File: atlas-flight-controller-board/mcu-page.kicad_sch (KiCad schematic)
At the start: 1 part

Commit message: finishing up schematic for v1.
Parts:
- renumbered U to U?
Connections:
- net SD_CS: now reaches U?.10 (CS1)
- net MOSI: now reaches U?.11 (MOSI)
- net MISO: now reaches U?.12 (MISO)
- net SCK: now reaches U?.13 (SCK)
- net UART_RFD900_TX_MCU_RX: now reaches U?.34 (RX8)
- net UART_MCU_TX_RFD900_RX: now reaches U?.35 (TX8)
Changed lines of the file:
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@@
 	(generator_version "9.0")
 	(paper "A4")
+	(global_label "UART_RFD900_TX_MCU_RX"
+		(shape input)
+		(at 124.46 83.82 180)
+		(fields_autoplaced yes)
+		(effects
+			(font
+				(size 1.27 1.27)
+			)
+			(justify right)
+		)
+		(property "Intersheetrefs" "${INTERSHEET_REFS}"
+			(at 96.9821 83.82 0)
+			(effects
+				(font
+					(size 1.27 1.27)
+				)
+				(justify right)
+				(hide yes)
+			)
+		)
+	)
+	(global_label "MOSI"
+		(shape input)
+		(at 165.1 101.6 0)
+		(fields_autoplaced yes)
+		(effects
+			(font
+				(size 1.27 1.27)
+			)
+			(justify left)
+		)
+		(property "Intersheetrefs" "${INTERSHEET_REFS}"
+			(at 172.6814 101.6 0)
+			(effects
+				(font
+					(size 1.27 1.27)
+				)
+				(justify left)
+				(hide yes)
+			)
+		)
+	)
 	(global_label "I2C_SDA"
 		(shape input)
@@
 		)
 	)
+	(global_label "UART_MCU_TX_RFD900_RX"
+		(shape input)
+		(at 124.46 86.36 180)
+		(fields_autoplaced yes)
+		(effects
+			(font
+				(size 1.27 1.27)
+			)
+			(justify right)
+		)
+		(property "Intersheetrefs" "${INTERSHEET_REFS}"
+			(at 96.9821 86.36 0)
+			(effects
+				(font
+					(size 1.27 1.27)
+				)
+				(justify right)
+				(hide yes)
+			)
+		)
+	)
 	(global_label "I2C_SCL"
 		(shape input)
@@
 				)
 				(justify right)
+				(hide yes)
+			)
+		)
+	)
+	(global_label "SCK"
+		(shape input)
+		(at 124.46 104.14 180)
+		(fields_autoplaced yes)
+		(effects
+			(font
+				(size 1.27 1.27)
+			)
+			(justify right)
+		)
+		(property "Intersheetrefs" "${INTERSHEET_REFS}"
+			(at 117.7253 104.14 0)
+			(effects
+				(font
+					(size 1.27 1.27)
+				)
+				(justify right)
+				(hide yes)
+			)
+		)
+	)
+	(global_label "MISO"
+		(shape input)
+		(at 165.1 99.06 0)
+		(fields_autoplaced yes)
+		(effects
+			(font
+				(size 1.27 1.27)
+			)
+			(justify left)
+		)
+		(property "Intersheetrefs" "${INTERSHEET_REFS}"
+			(at 172.6814 99.06 0)
+			(effects
+				(font
+					(size 1.27 1.27)
+				)
+				(justify left)
+				(hide yes)
+			)
+		)
+	)
+	(global_label "SD_CS"
+		(shape input)
+		(at 165.1 93.98 0)
+		(fields_autoplaced yes)
+		(effects
+			(font
+				(size 1.27 1.27)
+			)
+			(justify left)
+		)
+		(property "Intersheetrefs" "${INTERSHEET_REFS}"
+			(at 174.0118 93.98 0)
+			(effects
+				(font
+					(size 1.27 1.27)
+				)
+				(justify left)
 				(hide yes)
 			)
@@
 		(dnp no)
 		(fields_autoplaced yes)
-		(property "Reference" "U"
+		(property "Reference" "U?"
 			(at 144.78 33.02 0)
 			(effects
@@
 		(instances
 			(project "atlas-flight-controller-board"
-				(path "/99efb2d6-b5f7-438c-9ed2-f359400f01a1/0e8824f2-4013-4596-998b-cdfa7c1cf328"
-					(reference "U3")
+				(path "/99efb2d6-b5f7-438c-9ed2-f359400f01a1/ebeff960-adac-492b-ba2d-f8a8dedd6bc1"
+					(reference "U?")
 					(unit 1)
 				)

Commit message: wip commit
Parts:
- added J1: UART8 RPI Screw Term, TerminalBlock:TerminalBlock_Xinya_XY308-2.54-2P_1x02_P2.54mm_Horizontal, symbol Connector:Screw_Terminal_01x02
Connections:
- net UART_MCU_TX_RFD900_RX: now also U?.29 (TX7); no longer U?.35 (TX8)
- net UART_RFD900_TX_MCU_RX: now also U?.28 (RX7); no longer U?.34 (RX8)
- net UART_GPS_TX_MCU_RX: now reaches U?.0 (RX1)
- net UART_MCU_TX_GPS_RX: now reaches U?.1 (TX1)
- net GPS_FIX: now reaches U?.2 (OUT2)
- net MAG_INT: now reaches U?.20 (A6)
- net BARO_INT: now reaches U?.21 (A7)
- net IMU_INT1: now reaches U?.22 (A8)
- net IMU_INT2: now reaches U?.23 (A9)
- new net UART_MCU_TX_RPI_RX: J1.1 (Pin_1), U?.35 (TX8)
- new net UART_RPI_TX_MCU_RX: J1.2 (Pin_2), U?.34 (RX8)

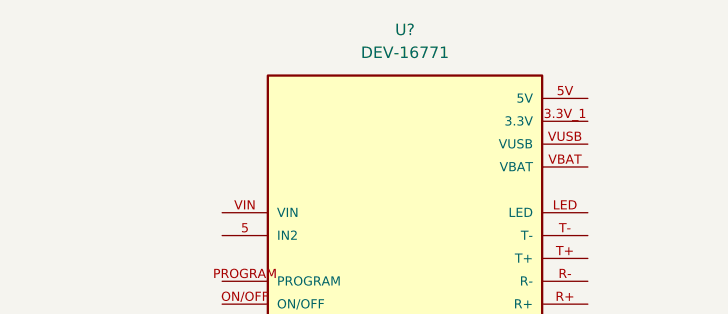
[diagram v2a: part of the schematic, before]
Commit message: Added Regulator, Leaving disconnected, and off pcb for now as teensy board does this automatically. Leaving on for future revs without teensy board
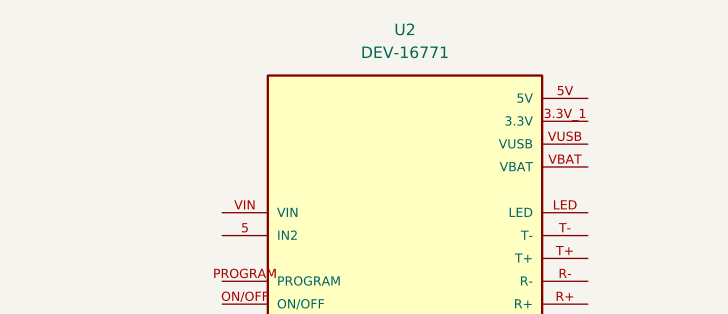
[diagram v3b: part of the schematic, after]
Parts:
- U2: renamed from U?; footprint DEV-16771:MODULE_DEV-16771 -> Teensy4.1:MODULE_DEV-16771
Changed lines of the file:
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@@
 		(dnp no)
 		(fields_autoplaced yes)
-		(property "Reference" "U?"
+		(property "Reference" "U2"
 			(at 144.78 33.02 0)
 			(effects
@@
 			)
 		)
-		(property "Footprint" "DEV-16771:MODULE_DEV-16771"
+		(property "Footprint" "Teensy4.1:MODULE_DEV-16771"
 			(at 144.78 88.9 0)
 			(effects
@@
 			(project "atlas-flight-controller-board"
 				(path "/99efb2d6-b5f7-438c-9ed2-f359400f01a1/ebeff960-adac-492b-ba2d-f8a8dedd6bc1"
-					(reference "U?")
+					(reference "U2")
 					(unit 1)
 				)

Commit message: Updating IMU to SPI
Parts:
- removed J1: UART8 RPI Screw Term, TerminalBlock:TerminalBlock_Xinya_XY308-2.54-2P_1x02_P2.54mm_Horizontal, symbol Connector:Screw_Terminal_01x02
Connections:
- net UART_MCU_TX_RPI_RX: no longer names the net of U2.35 (TX8)
- net UART_RPI_TX_MCU_RX: no longer names the net of U2.34 (RX8)
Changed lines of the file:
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@@
 	(generator_version "9.0")
 	(paper "A4")
-	(junction
-		(at 124.46 83.82)
-		(diameter 0)
-		(color 0 0 0 0)
-	)
-	(junction
-		(at 124.46 86.36)
-		(diameter 0)
-		(color 0 0 0 0)
-	)
 	(wire
 		(pts
-			(xy 74.93 86.36) (xy 124.46 86.36)
+			(xy 129.54 83.82) (xy 124.46 83.82)
 		)
 		(stroke
@@
 	(wire
 		(pts
-			(xy 129.54 83.82) (xy 124.46 83.82)
+			(xy 129.54 86.36) (xy 124.46 86.36)
 		)
 		(stroke
 			(width 0)
 			(type default)
-		)
-	)
-	(wire
-		(pts
-			(xy 129.54 86.36) (xy 124.46 86.36)
-		)
-		(stroke
-			(width 0)
-			(type default)
-		)
-	)
-	(wire
-		(pts
-			(xy 74.93 83.82) (xy 124.46 83.82)
-		)
-		(stroke
-			(width 0)
-			(type default)
-		)
-	)
-	(label "UART_MCU_TX_RPI_RX"
-		(at 74.93 86.36 0)
-		(effects
-			(font
-				(size 1.27 1.27)
-			)
-			(justify left bottom)
-		)
-	)
-	(label "UART_RPI_TX_MCU_RX"
-		(at 74.93 83.82 0)
-		(effects
-			(font
-				(size 1.27 1.27)
-			)
-			(justify left bottom)
 		)
 	)
@@
 					(unit 1)
 				)
-			)
-		)
-	)
-	(symbol
-		(lib_id "Connector:Screw_Terminal_01x02")
-		(at 69.85 86.36 180)
-		(unit 1)
-		(exclude_from_sim no)
-		(in_bom yes)
-		(on_board yes)
-		(dnp no)
-		(property "Reference" "J1"
-			(at 69.85 76.454 0)
-			(effects
-				(font
-					(size 1.27 1.27)
-				)
-			)
-		)
-		(property "Value" "UART8 RPI Screw Term"
-			(at 69.85 78.994 0)
-			(effects
-				(font
-					(size 1.27 1.27)
-				)
-			)
-		)
-		(property "Footprint" "TerminalBlock:TerminalBlock_Xinya_XY308-2.54-2P_1x02_P2.54mm_Horizontal"
-			(at 69.85 86.36 0)
-			(effects
-				(font
-					(size 1.27 1.27)
-				)
-				(hide yes)
-			)
-		)
-		(property "Datasheet" "~"
-			(at 69.85 86.36 0)
-			(effects
-				(font
-					(size 1.27 1.27)
-				)
-				(hide yes)
-			)
-		)
-		(property "Description" "Generic screw terminal, single row, 01x02, script generated (kicad-library-utils/schlib/autogen/connector/)"
-			(at 69.85 86.36 0)
-			(show_name yes)
-			(effects
-				(font
-					(size 1.27 1.27)
-				)
-				(hide yes)
-			)
-		)
-		(pin "2"
-		)
-		(pin "1"
-		)
-		(instances
-			(project ""
-				(path "/99efb2d6-b5f7-438c-9ed2-f359400f01a1/ebeff960-adac-492b-ba2d-f8a8dedd6bc1"
-					(reference "J1")
-					(unit 1)
-				)

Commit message: Wip commit
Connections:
- net I2C_SCL: no longer names the net of U2.19 (A5)
- net I2C_SDA: no longer names the net of U2.18 (A4)
- net MAG_INT: no longer names the net of U2.20 (A6)
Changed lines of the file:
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@@
-		)
-	)
-	(global_label "MAG_INT"
-		(shape input)
-		(at 124.46 124.46 180)
-		(fields_autoplaced yes)
-		(effects
-			(font
-				(size 1.27 1.27)
-			)
-			(justify right)
-		)
-		(property "Intersheetrefs" "${INTERSHEET_REFS}"
-			(at 113.7943 124.46 0)
-			(effects
-				(font
-					(size 1.27 1.27)
-				)
-				(justify right)
-				(hide yes)
-			)
 		)
 	)
@@
 		)
 	)
-	(global_label "I2C_SDA"
-		(shape input)
-		(at 124.46 119.38 180)
-		(fields_autoplaced yes)
-		(effects
-			(font
-				(size 1.27 1.27)
-			)
-			(justify right)
-		)
-		(property "Intersheetrefs" "${INTERSHEET_REFS}"
-			(at 113.8548 119.38 0)
-			(effects
-				(font
-					(size 1.27 1.27)
-				)
-				(justify right)
-				(hide yes)
-			)
-		)
-	)
 	(global_label "BARO_INT"
 		(shape input)
@@
 			(effects
 				(font
-					(size 1.27 1.27)
-				)
-				(justify right)
-				(hide yes)
-			)
-		)
-	)
-	(global_label "I2C_SCL"
-		(shape input)
-		(at 124.46 121.92 180)
-		(fields_autoplaced yes)
-		(effects
-			(font
-				(size 1.27 1.27)
-			)
-			(justify right)
-		)
-		(property "Intersheetrefs" "${INTERSHEET_REFS}"
-			(at 113.9153 121.92 0)
-			(effects
-				(font

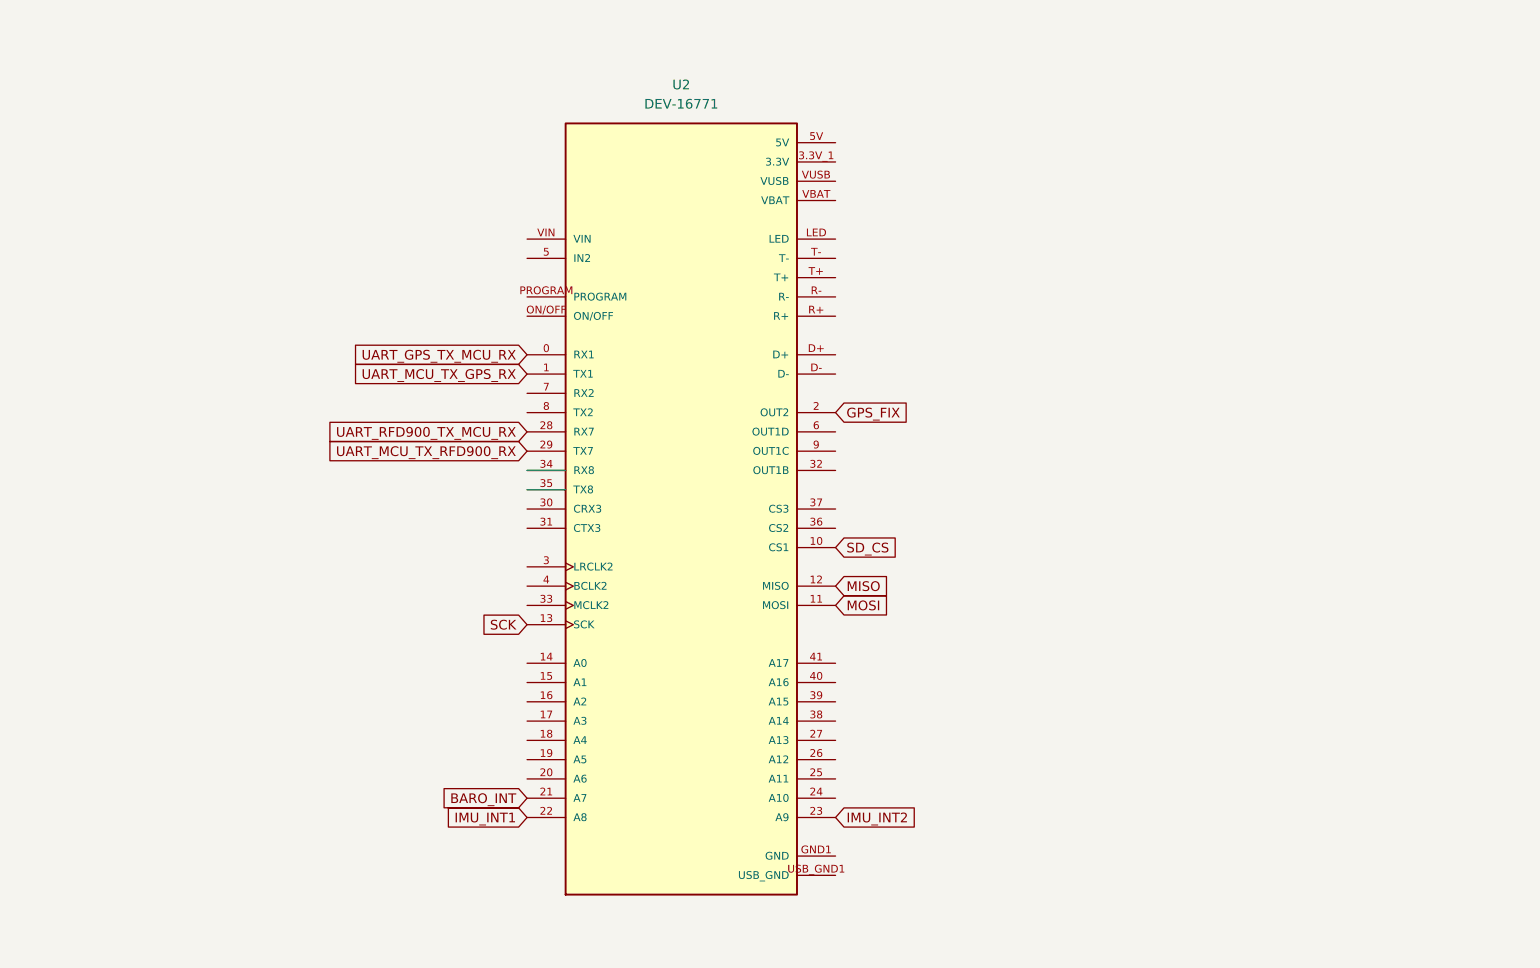
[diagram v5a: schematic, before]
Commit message: Bare Schematic (No LEDS, etc added) finished. Begin PCB Layout.
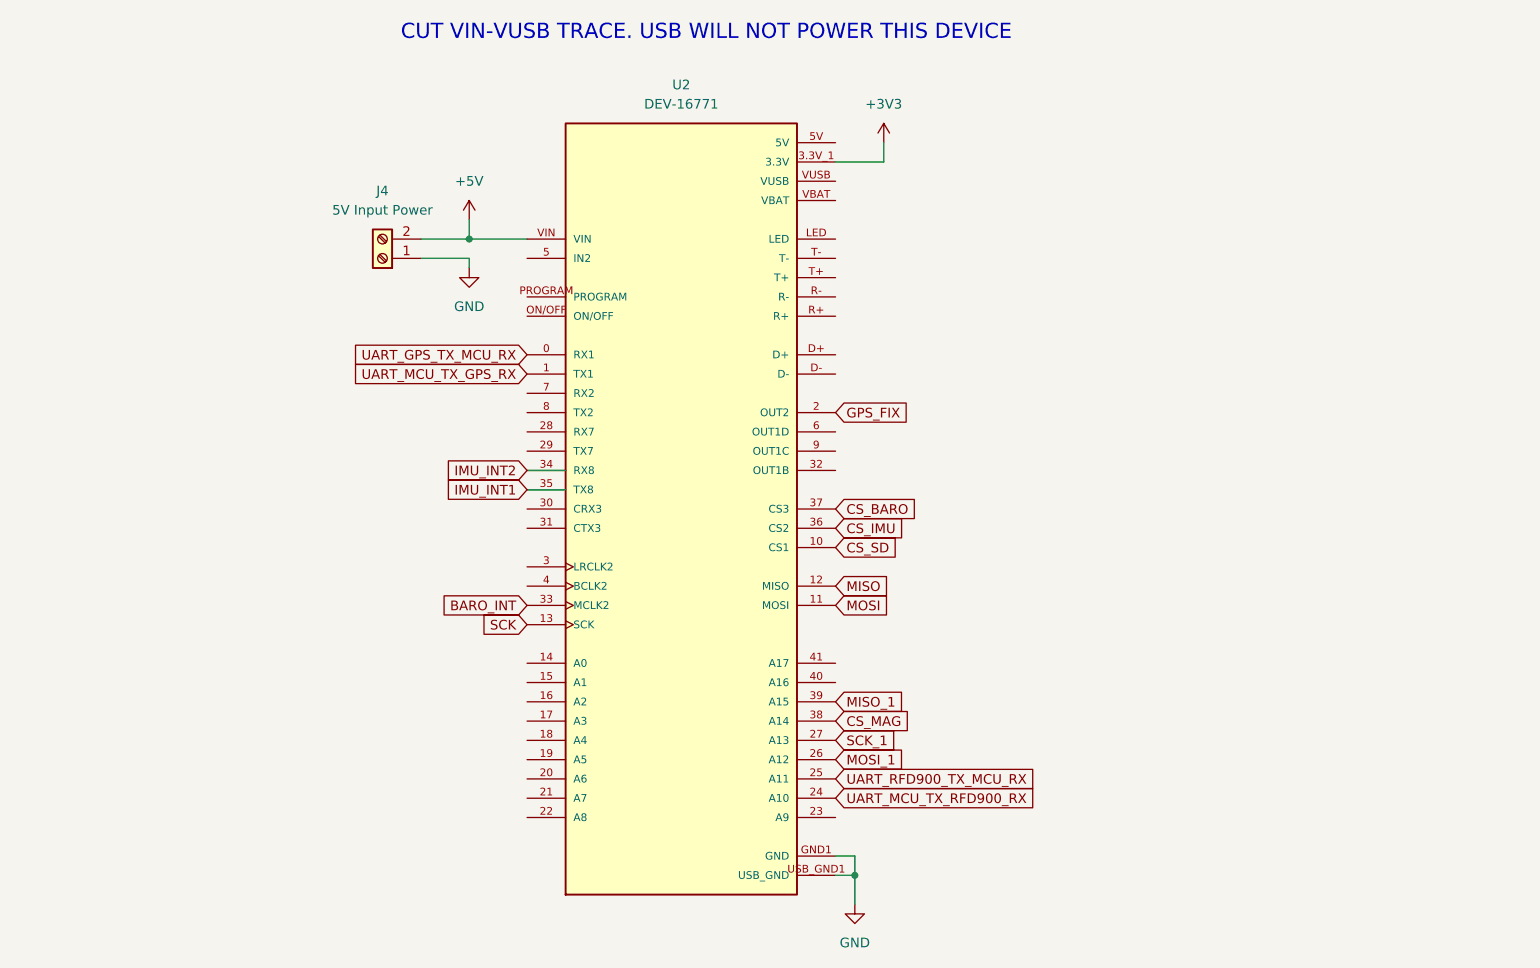
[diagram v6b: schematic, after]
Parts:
- added J4: 5V Input Power, TerminalBlock:TerminalBlock_Xinya_XY308-2.54-2P_1x02_P2.54mm_Horizontal, symbol Connector:Screw_Terminal_01x02
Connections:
- net USB_GND is gone; now on net GND: U2.USB_GND1 (USB_GND), U2.USB_GND2 (USB_GND)
- net BARO_INT: now also U2.33 (MCLK2); no longer U2.21 (A7)
- net GND: now also J4.1 (Pin_1)
- net IMU_INT1: now also U2.35 (TX8); no longer U2.22 (A8)
- net IMU_INT2: now also U2.34 (RX8); no longer U2.23 (A9)
- net UART_MCU_TX_RFD900_RX: now also U2.24 (A10); no longer U2.29 (TX7)
- net UART_RFD900_TX_MCU_RX: now also U2.25 (A11); no longer U2.28 (RX7)
- net MOSI_1: now reaches U2.26 (A12)
- net SCK_1: now reaches U2.27 (A13)
- net CS_IMU: now reaches U2.36 (CS2)
- net CS_BARO: now reaches U2.37 (CS3)
- net CS_MAG: now reaches U2.38 (A14)
- net MISO_1: now reaches U2.39 (A15)
- net +5V: now reaches U2.VIN
- net +5V: now also J4.2 (Pin_2)
- net 3.3V renamed +3V3
- net SD_CS renamed CS_SD
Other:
- note added: "CUT VIN-VUSB TRACE. USB WILL NOT POWER THIS DEVICE"

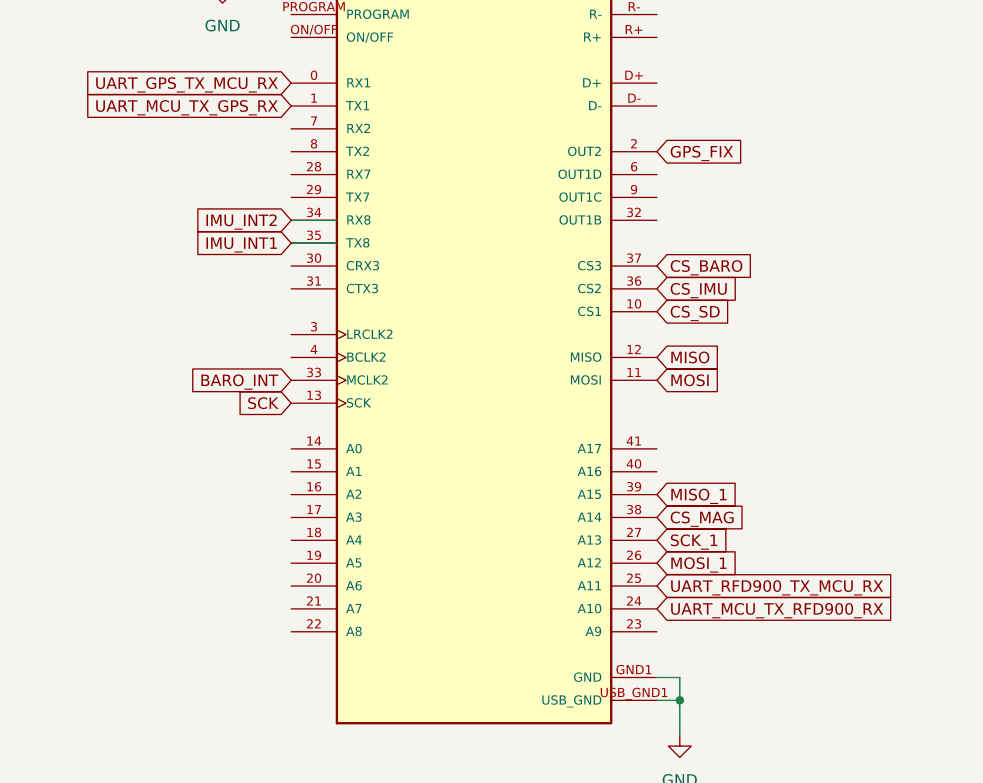
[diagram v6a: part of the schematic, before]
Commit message: Sensor and Flash layout finished besides MISO, MOSI resistors (reduce ringing). Added plated M2 mounting holes.
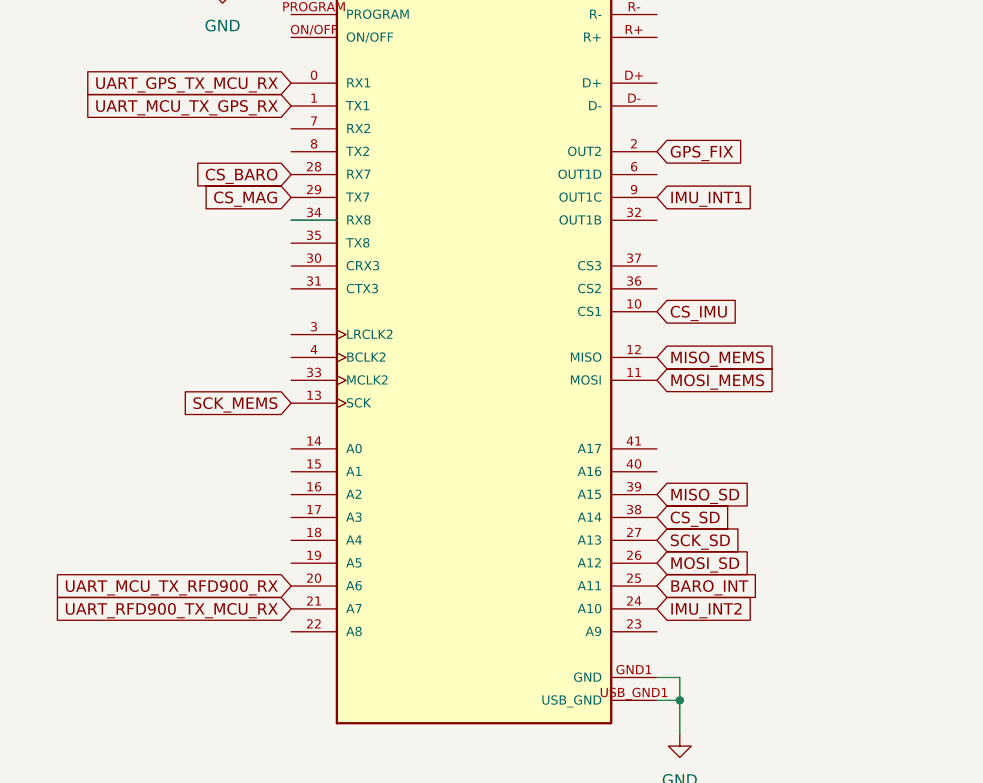
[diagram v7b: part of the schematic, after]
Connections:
- net BARO_INT: now also U2.25 (A11); no longer U2.33 (MCLK2)
- net CS_BARO: now also U2.28 (RX7); no longer U2.37 (CS3)
- net CS_IMU: now also U2.10 (CS1); no longer U2.36 (CS2)
- net CS_MAG: now also U2.29 (TX7); no longer U2.38 (A14)
- net CS_SD: now also U2.38 (A14); no longer U2.10 (CS1)
- net IMU_INT1: now also U2.9 (OUT1C); no longer U2.35 (TX8)
- net IMU_INT2: now also U2.24 (A10); no longer U2.34 (RX8)
- net UART_MCU_TX_RFD900_RX: now also U2.20 (A6); no longer U2.24 (A10)
- net UART_RFD900_TX_MCU_RX: now also U2.21 (A7); no longer U2.25 (A11)
- net MISO renamed MISO_MEMS
- net MISO_1 renamed MISO_SD
- net MOSI renamed MOSI_MEMS
- net MOSI_1 renamed MOSI_SD
- net SCK renamed SCK_MEMS
- net SCK_1 renamed SCK_SD
